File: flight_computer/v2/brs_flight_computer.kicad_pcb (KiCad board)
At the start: 4 copper layers, 81.1 x 75 mm, 265 parts, among them J1 Conn_01x05_Male, J10 Perovskite 3, J11 GaAs Panel, J12 GaAs Temperature, J13 Perovskite 1, J14 Perovskite 2, J15 Power, J16 Power, J17 Power, J18 Power, J19 Power, J2 Conn_01x05_Male, J20 BUSS+, J21 EPS Serial, J22 Power, J3 Conn_01x10_Male, J5 Panel 3, J8 Conn_01x03_Male, J9 0781710004, Q1 BSS138, Q2 BSS138, Q3 BSS138, U1 OPA2387, U10 TLV7031DBV, U11 INA190A4IDDFR, U12 INA190A4IDDFR, U13 INA190A4IDDFR, U14 INA190A4IDDFR, U17 INA190A4IDDFR, U18 ADG841YKSZ-500RL7, U19 ADG841YKSZ-500RL7, U2 OPA2387, U20 ADG841YKSZ-500RL7, U21 CD4516B_PW_16, U22 ADG841YKSZ-500RL7, U23 ADG841YKSZ-500RL7, U24 ADG841YKSZ-500RL7, U25 ADG841YKSZ-500RL7, U26 CD4516B_PW_16, U27 ADG841YKSZ-500RL7, U28 ADG841YKSZ-500RL7, U29 ADG841YKSZ-500RL7, U3 TLV7031DBV, U30 ADG841YKSZ-500RL7, U31 CD4516B_PW_16, U32 ADG841YKSZ-500RL7, U33 ADG841YKSZ-500RL7, U34 ADG841YKSZ-500RL7, U35 ADG841YKSZ-500RL7, U36 CD4516B_PW_16, U37 ADG841YKSZ-500RL7, U38 CD4518BM96, U39 74AHC1G08, U4 4012, U40 CD4514BM, U41 CD4514BM, U42 ADG839YKSZ-REEL7, U43 ADG839YKSZ-REEL7, U44 ADG839YKSZ-REEL7, U45 ADG839YKSZ-REEL7, U46 ADG839YKSZ-REEL7, U47 ADG839YKSZ-REEL7, U48 ADG839YKSZ-REEL7, U49 ADG839YKSZ-REEL7, U5 4012, U50 ADG839YKSZ-REEL7, U51 ADG839YKSZ-REEL7, U52 ADG839YKSZ-REEL7, U53 ADG839YKSZ-REEL7, U54 ADG839YKSZ-REEL7, U55 ADG839YKSZ-REEL7, U56 ADG839YKSZ-REEL7, U57 ADG839YKSZ-REEL7, U58 ADG839YKSZ-REEL7, U59 ADG839YKSZ-REEL7, U6 4012, U7 LT6654AHS6-3.3, U8 MSP430FR5969IRGZR, U9 SN74CBT3253, Y1 CM8V-T1A

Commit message: Finished layout of flight computer
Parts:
- removed C102: 10u, Capacitor_SMD:C_0603_1608Metric
- removed C103, C72, C73, C87, C94, C95, C98: 0.1u, Capacitor_SMD:C_0603_1608Metric
- removed C49, C50: 1u, Capacitor_SMD:C_0603_1608Metric
- removed J17: Power, Connector_Hirose:Hirose_DF13C_CL535-0402-2-51_1x02-1MP_P1.25mm_Vertical
- removed R53, R54: 4k7, Resistor_SMD:R_0603_1608Metric
- removed TP19, TP21: Voltage Test-, TestPoint:TestPoint_Pad_1.0x1.0mm
- removed U4, U5: 4012, Package_SO:TSSOP-14_4.4x5mm_P0.65mm
- added C28: 0.1u, Capacitor_SMD:C_0603_1608Metric, B.Cu at (116.1, 93.5)
- added C29: 0.1u, Capacitor_SMD:C_0603_1608Metric, B.Cu at (116.1, 126.5)
- C1, C10, C100, C101, C104, C106, C107, C109, C11, C110, C14, C15, C16, C17, C19, C2, C20, C21, C22, C23, C3, C4, C46, C47, C48, C5, C51, C52, C53, C54, C55, C56, C57, C58, C59, C6, C60, C61, C62, C63, C64, C65, C66, C67, C68, C69, C7, C70, C71, C74, C75, C76, C77, C78, C79, C80, C81, C82, C83, C84, C85, C86, C88, C89, C9, C90, C91, C92, C93, C96, C97, C99, R1, R2, R3, R71, R72, R73: moved to B.Cu
- TP11: value Voltage Test- -> I
- TP9: value Voltage Test- -> Voltage Test+
- moved C17 319.1 mm to (116.1, 110.0)
- moved C14 287.4 mm to (150.6, 130.2), turned to 270 degrees
- moved C23 284.6 mm to (150.6, 112.0), turned to 270 degrees
- moved C21 280.3 mm to (150.9, 97.2), turned to 180 degrees
- moved C22 279.4 mm to (150.6, 87.2), turned to 270 degrees
- moved C20 279.4 mm to (150.9, 135.6), turned to 90 degrees
- moved C15 276.9 mm to (150.6, 105.5), turned to 270 degrees
- moved C19 275.1 mm to (150.9, 121.5), turned to 180 degrees
- moved C16 264.0 mm to (168.3, 98.6)
- moved C66 259.8 mm to (160.7, 136.5), turned to 180 degrees
- moved C51 255.0 mm to (160.7, 90.8), turned to 180 degrees
- moved C59 254.8 mm to (160.7, 103.0), turned to 180 degrees
- moved C57 254.8 mm to (160.7, 99.9), turned to 180 degrees
- moved C54 254.5 mm to (160.7, 121.3), turned to 180 degrees
- moved C62 250.6 mm to (160.7, 133.5), turned to 180 degrees
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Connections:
- net /Ground Switcher/PEROVSKITE_1_POS renamed P1_CP
- net /Ground Switcher/PEROVSKITE_2_POS renamed P2_CP
- net /Ground Switcher/PEROVSKITE_3_POS renamed P3_CP
- net Net-(J10-Pad1) renamed P3_P4
- net Net-(J10-Pad2) renamed P3_P5
- net Net-(J10-Pad3) renamed P3_P6
- net Net-(J10-Pad4) renamed P3_P3
- net Net-(J10-Pad5) renamed P3_P2
- net Net-(J10-Pad6) renamed P3_P1
- net Net-(J13-Pad3) renamed P1_P6
- net Net-(J13-Pad4) renamed P1_P3
- net Net-(J13-Pad5) renamed P1_P2
- net Net-(J13-Pad6) renamed P1_P1
- net Net-(J14-Pad1) renamed P2_P4
- net Net-(J14-Pad3) renamed P2_P6
- C101 pad 1: VDDF -> VPP
- C14 pad 1: VBUS -> +3V3
- C16 pad 1: VBUS -> +3V3
- C18 pad 1: VBUS -> GND
- C18 pad 2: GND -> +3V3
- C20 pad 1: VBUS -> +3V3
- C21 pad 1: VBUS -> +3V3
- C58 pad 1: VBUS -> +3V3
- C60 pad 1: VBUS -> +3V3
- C62 pad 1: VBUS -> +3V3
- C65 pad 1: VBUS -> +3V3
- C66 pad 1: VBUS -> +3V3
- J1 pad 2: TEST -> RX_IN
- J1 pad 3: PAYLOAD_RST -> TX_OUT
- J13 pad 1: Net-(J13-Pad1) -> P1_P4
- J13 pad 2: Net-(J13-Pad2) -> P1_P5
- J14 pad 2: Net-(J14-Pad2) -> P2_P5
- J14 pad 4: Net-(J14-Pad4) -> P2_P3
- J14 pad 5: Net-(J14-Pad5) -> P2_P2
- J14 pad 6: Net-(J14-Pad6) -> P2_P1
- J2 pad 3: RX_IN -> TEST
- J2 pad 4: TX_OUT -> PAYLOAD_RST
- J3 pad 10: /Microcontroller/NO_V -> /Microcontroller/NC_V
- J3 pad 9: /Microcontroller/NC_V -> /Microcontroller/NO_V
- TP11 pad 1: GND -> Net-(R42-Pad2)
- TP9 pad 1: GND -> Net-(R4-Pad2)
- U42 pad 5: Net-(J13-Pad1) -> P1_P5
- U43 pad 5: Net-(J13-Pad2) -> P1_P4
- U49 pad 5: Net-(J14-Pad2) -> P2_P3
- U51 pad 5: Net-(J14-Pad4) -> P2_P5
- U52 pad 5: Net-(J14-Pad5) -> P2_P1
- U53 pad 5: Net-(J14-Pad6) -> P2_P2
- U6 pad 2: Net-(U5-Pad13) -> Net-(U36-Pad6)
- U6 pad 3: Net-(U5-Pad1) -> Net-(U31-Pad6)
- U6 pad 4: Net-(U4-Pad13) -> Net-(U26-Pad6)
- U6 pad 5: Net-(U4-Pad1) -> Net-(U21-Pad6)
- U8 pad 26: /Microcontroller/SET -> Net-(U8-Pad26)
- U8 pad 27: /Curve Tracer/S1_CT -> /Microcontroller/CT_GOOD
- U8 pad 29: /Ground Switcher/MUX_CLOCK -> /Ground Switcher/MUX_GOOD
- U8 pad 30: /Microcontroller/MAG_INT -> /Ground Switcher/MUX_CLOCK
- U8 pad 33: /EPS Connections/BUSY -> /Ground Switcher/GAAS_TEMP
- U8 pad 34: /Ground Switcher/MUX_GOOD -> /EPS Connections/BUSY
- U8 pad 35: /Ground Switcher/GAAS_TEMP -> /Passive ADCS/PANEL_3_CURRENT
- U8 pad 39: /Microcontroller/UNSET -> Net-(U8-Pad39)
- U8 pad 4: /Microcontroller/PANEL_1_ON -> /Microcontroller/NO_V
- U8 pad 5: /Microcontroller/PANEL_2_ON -> /Microcontroller/UNSET
- U8 pad 6: /Passive ADCS/PANEL_3_CURRENT -> /Microcontroller/SET
- U8 pad 7: /Curve Tracer/S0_CT -> /Microcontroller/MAG_INT
- U8 pad 8: /Microcontroller/CT_GOOD -> /Curve Tracer/S0_CT
- U8 pad 9: /Microcontroller/NO_V -> /Curve Tracer/S1_CT
- U9 pad 11: P_1_VOLTAGE -> P_3_VOLTAGE
- U9 pad 13: P_3_VOLTAGE -> P_1_VOLTAGE
- U9 pad 3: P_3_CURRENT -> P_1_CURRENT
- U9 pad 5: P_1_CURRENT -> P_3_CURRENT
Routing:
- net GND: track 0.00 -> 214.6 mm, vias 0 -> 90
- net /Ground Switcher/SCL: track 0.00 -> 156.1 mm, vias 0 -> 2
- net /Ground Switcher/SDA: track 0.00 -> 153.2 mm, vias 0 -> 2
- net VBUS: track 0.00 -> 152.1 mm, vias 0 -> 59
- net /Ground Switcher/MUX_CLOCK: track 0.00 -> 109.0 mm, vias 0 -> 2
- net /Ground Switcher/MUX_GOOD: track 0.00 -> 92.8 mm, vias 0 -> 2
- net +3V3: track 0.00 -> 91.3 mm, vias 0 -> 26
- net /Ground Switcher/GAAS_TEMP: track 0.00 -> 90.4 mm, vias 0 -> 2
- net GAAS_CURRENT: track 0.00 -> 86.8 mm, vias 0 -> 2
- net P1_CP: track 0.00 -> 81.0 mm
- net GAAS_VOLTAGE: track 0.00 -> 79.4 mm, vias 0 -> 2
- net P_3_VOLTAGE: track 0.00 -> 71.7 mm, vias 0 -> 2
- net P2_CP: track 0.00 -> 65.9 mm
- net P_3_CURRENT: track 0.00 -> 62.6 mm, vias 0 -> 2
- net Net-(R17-Pad1): track 0.00 -> 60.8 mm, vias 0 -> 1
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- added copper zone on In1.Cu, net +3V3
- added copper zone on In2.Cu, net +3V3
- added copper zone on B.Cu, net GND
- added copper zone on F.Cu, net GND
- added copper zone on In1.Cu, net VBUS
- added copper zone on In2.Cu, net VBUS

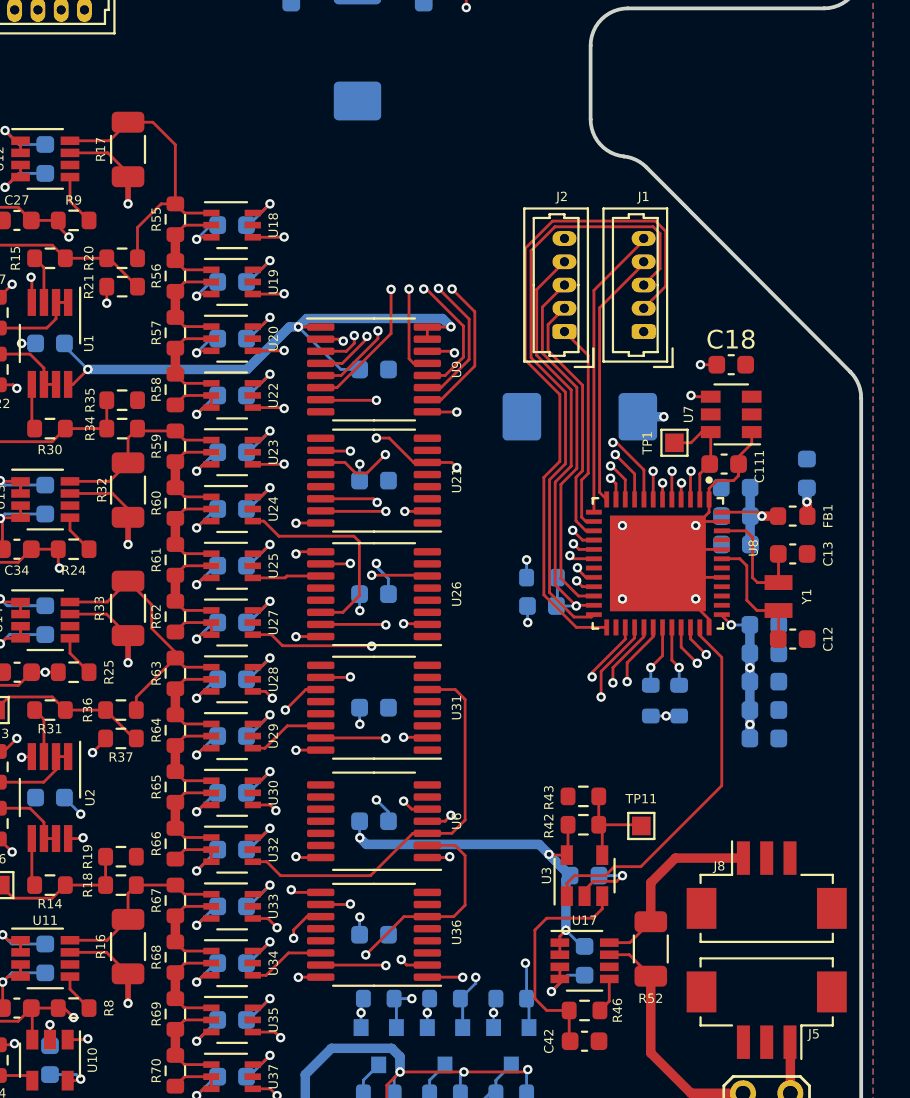
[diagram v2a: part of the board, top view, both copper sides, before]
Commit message: Create v3 flight computer
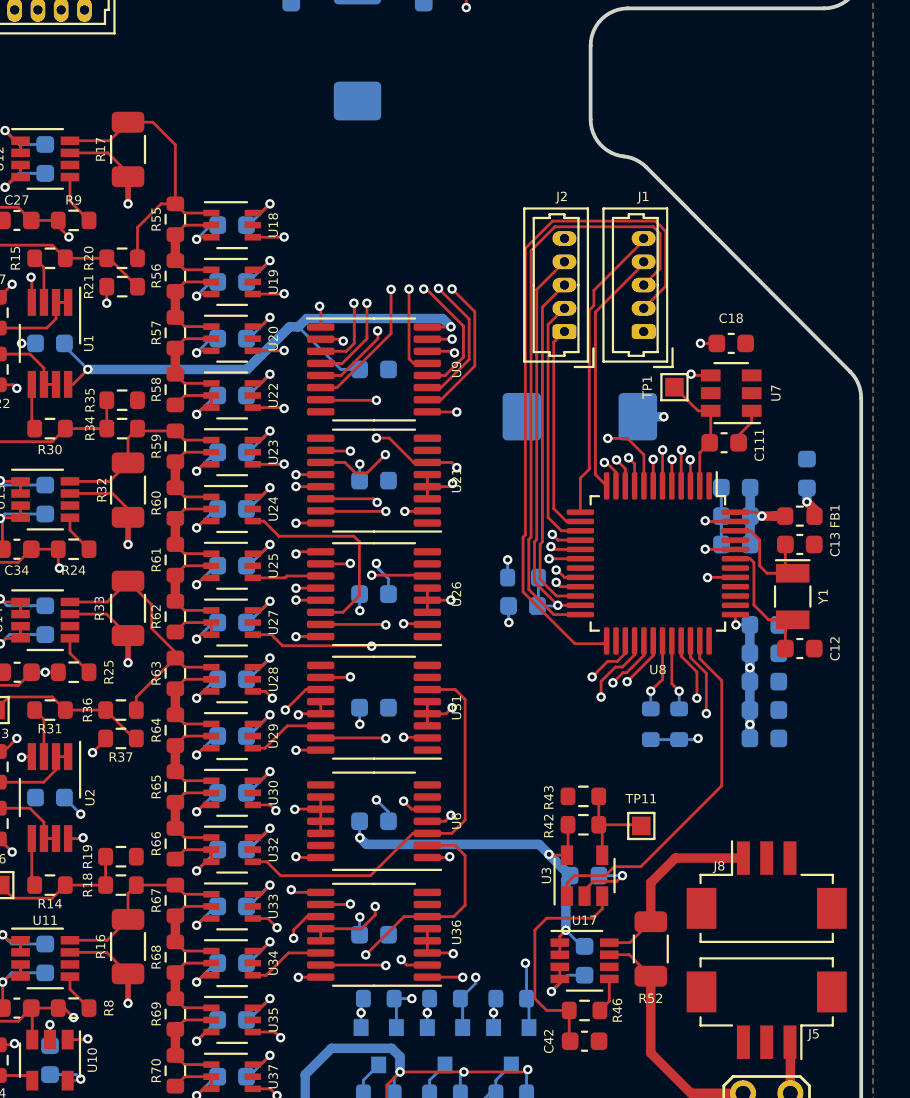
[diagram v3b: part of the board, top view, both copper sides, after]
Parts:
- R55, R59, R63, R67: value 1M -> 120
- R56, R60, R64, R68: value 250 -> 270
- R57, R61, R65, R69: value 500 -> 430
- U8: footprint MSP430FR5969IRGZR:QFN50P700X700X100-49N -> Package_QFP:LQFP-48_7x7mm_P0.5mm
- Y1: footprint CM8V-T1A-32:XTAL_CM8V-T1A-32.768KHZ-7PF-20PPM-TA-QC -> Crystal:Crystal_SMD_MicroCrystal_CC7V-T1A-2Pin_3.2x1.5mm
- moved TP1 2.98 mm to (184.4, 99.5)
- moved R1 1.27 mm to (183.1, 117.6)
- moved R2 1.27 mm to (184.7, 117.6)
- moved C111 1.14 mm to (187.1, 102.5)
- moved C18 1.14 mm to (187.5, 97.2)
- moved U7 1.14 mm to (187.5, 99.8)
- moved C2 1.02 mm to (176.3, 111.3)
- moved R3 1.02 mm to (176.3, 109.7)
- moved Y1 0.76 mm to (190.8, 110.7)
- moved C12 0.63 mm to (191.1, 113.5)
- moved C13 0.63 mm to (191.1, 108.0)
- moved FB1 0.38 mm to (191.1, 106.4)
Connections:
- U21 pad 12: Net-(U21-Pad12) -> GND
- U21 pad 13: Net-(U21-Pad13) -> GND
- U21 pad 3: Net-(U21-Pad3) -> GND
- U21 pad 4: Net-(U21-Pad4) -> GND
- U21 pad 5: Net-(U21-Pad5) -> GND
- U26 pad 12: Net-(U26-Pad12) -> GND
- U26 pad 13: Net-(U26-Pad13) -> GND
- U26 pad 3: Net-(U26-Pad3) -> GND
- U26 pad 4: Net-(U26-Pad4) -> GND
- U26 pad 5: Net-(U26-Pad5) -> GND
- U31 pad 12: Net-(U31-Pad12) -> GND
- U31 pad 13: Net-(U31-Pad13) -> GND
- U31 pad 3: Net-(U31-Pad3) -> GND
- U31 pad 4: Net-(U31-Pad4) -> GND
- U31 pad 5: Net-(U31-Pad5) -> GND
- U36 pad 12: Net-(U36-Pad12) -> GND
- U36 pad 13: Net-(U36-Pad13) -> GND
- U36 pad 3: Net-(U36-Pad3) -> GND
- U36 pad 4: Net-(U36-Pad4) -> GND
- U36 pad 5: Net-(U36-Pad5) -> GND
- U6 pad 10: (no net) -> GND
- U6 pad 11: (no net) -> GND
- U6 pad 12: (no net) -> GND
- U6 pad 13: (no net) -> Net-(U6-Pad13)
- U6 pad 9: (no net) -> GND
- U9 pad 1: +3V3 -> GND
- U9 pad 15: +3V3 -> GND
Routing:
- net GND: track 214.6 -> 226.5 mm, vias 90 -> 102
- net /Ground Switcher/SDA: track 153.2 -> 155.0 mm
- net /Ground Switcher/SCL: track 156.1 -> 157.9 mm
- net +3V3: track 91.3 -> 90.2 mm, vias 26 -> 25
- net TEST: track 20.0 -> 18.9 mm
- net TX_OUT: track 33.2 -> 32.3 mm
- net /EPS Connections/TX: track 29.8 -> 28.9 mm
- net PAYLOAD_RST: track 24.3 -> 23.4 mm
- net Net-(C13-Pad2): track 7.00 -> 7.84 mm
- net /Microcontroller/LADDER_CLOCK: track 49.7 -> 48.9 mm
- net /EPS Connections/RX: track 33.0 -> 32.2 mm
- net /Curve Tracer/READ_VOLTAGE: track 13.2 -> 12.5 mm
- net /Ground Switcher/GAAS_TEMP: track 90.4 -> 89.7 mm
- net /EPS Connections/BUSY: track 29.7 -> 28.9 mm
- net /Ground Switcher/MUX_CLOCK: track 109.0 -> 108.2 mm
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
